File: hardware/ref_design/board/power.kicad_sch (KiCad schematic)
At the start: 25 parts, among them Q1 2N7002, U3 ME6211C33M5G

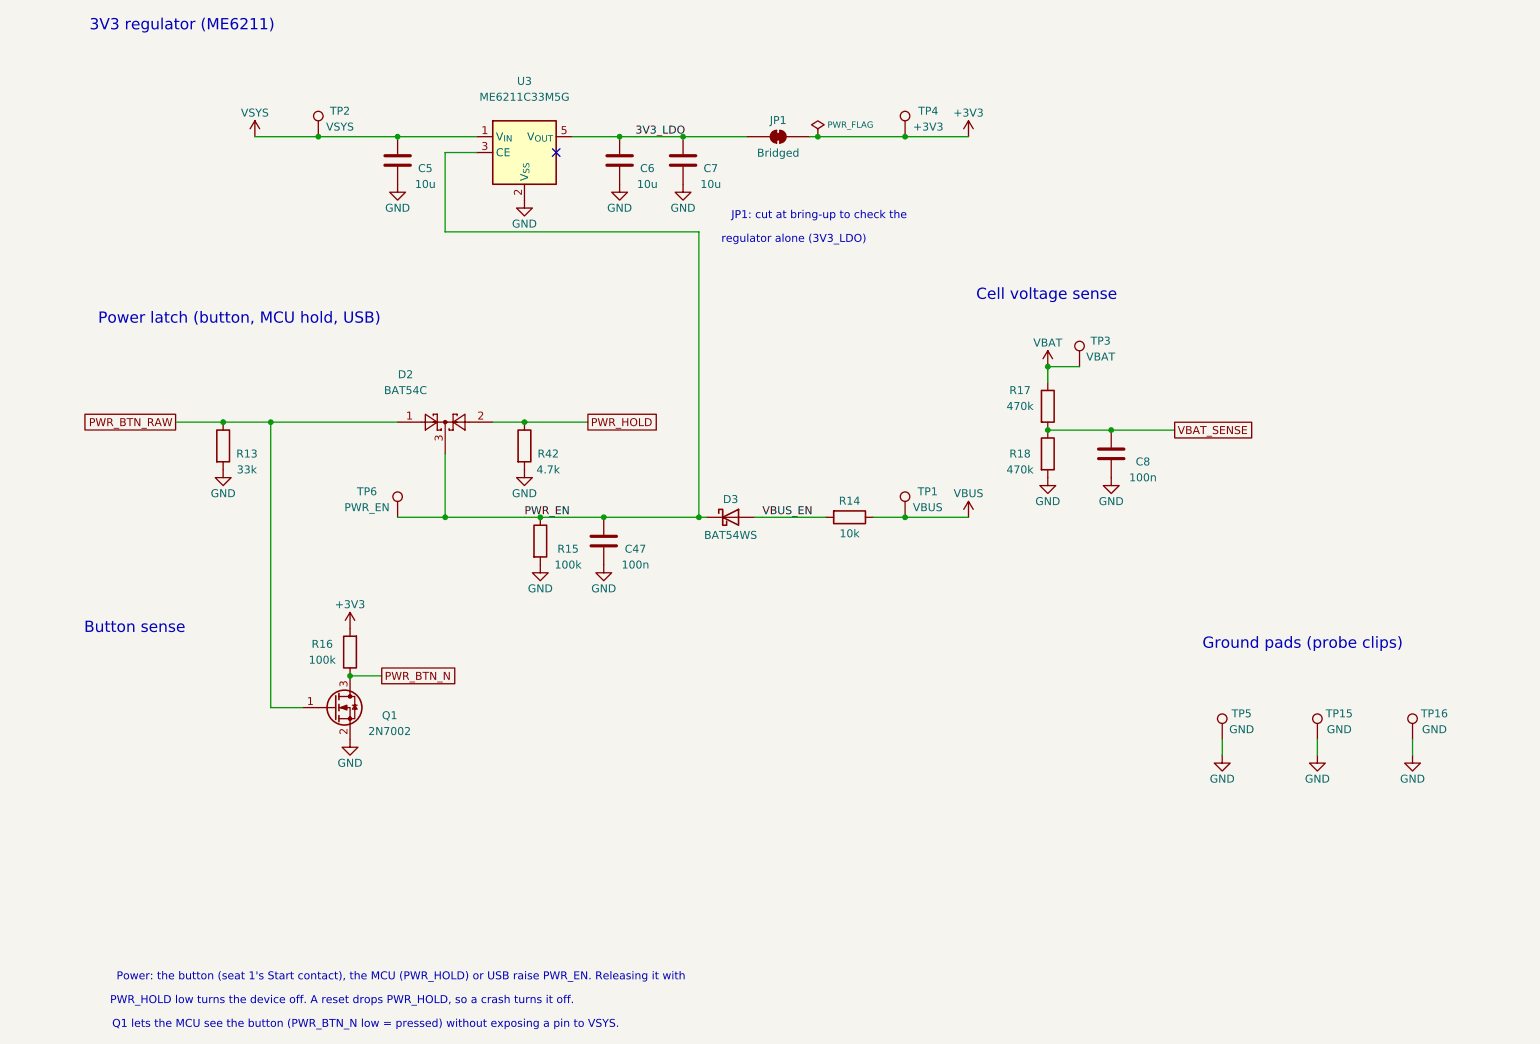
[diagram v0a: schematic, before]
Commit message: WIP: row 19 with shift registers and rows 1, 4, 16; 2 nets unrouted
The cell in a 54.0 x 37.0 mm hole, no speaker, every machine-placed part on
the top. New since the last WIP: each seat's D-pad and A/B/X/Y through a
74HC165 (SN74HC165PWR, chained, SR_PL/SR_CLK/SR_DATA on GPIO28-30, 10k
arrays); seat 2's Start powers on too (D8, R62, Q7, R63; P2_START on
GPIO34); Start/Select on 4 mm metal dome footprints; the BQ24073 power-path
charger in place of the TP4056 and its load sharing (pin reviews written);
the LDO beside the core; side screws at case (+-31.4, +-36); J1 at case
y -11. GPIO8 and GPIO11 (audio) unconnected.

Checks: check_netlist, check_pins and ERC pass (0). DRC: 0 errors, 8
cosmetic silkscreen warnings, 2 unconnected: QSPI_SS (U4 pin 75 to its
3.5 mm stub) and P1_SELECT (U4 pin 44 to SW20). check_fit: 17, all from
the case not knowing the moved screws, J1 and the dome vents yet.

Co-Authored-By: Claude Opus 5.5 <noreply@anthropic.com>
Claude-Session: https://claude.ai/code/session_01Y3mFMxLYqNeyyedvbYuRwX
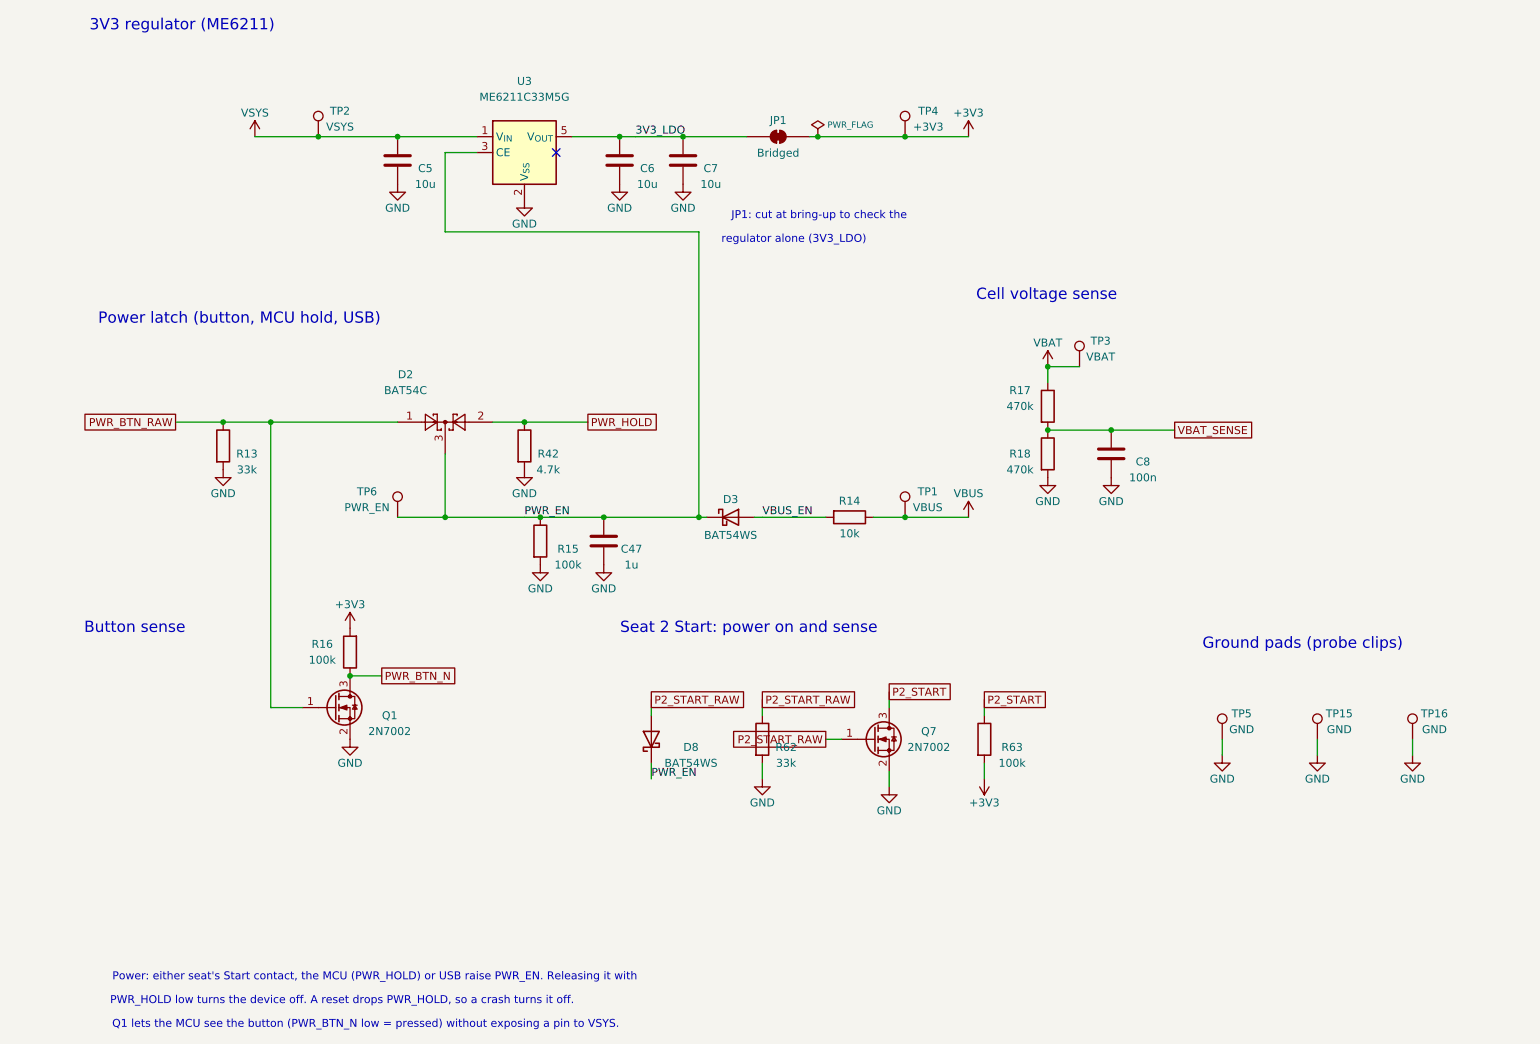
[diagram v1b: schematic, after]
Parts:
- added D8: BAT54WS, Diode_SMD:D_SOD-323, symbol Device:D_Schottky
- added Q7: 2N7002, Package_TO_SOT_SMD:SOT-23, symbol Transistor_FET:2N7002
- added R62: 33k, Resistor_SMD:R_0402_1005Metric, symbol Device:R
- added R63: 100k, Resistor_SMD:R_0402_1005Metric, symbol Device:R
- C47: value 100n -> 1u; LCSC C1525 -> C52923; MPN CL05B104KO5NNNC -> CL05A105KA5NQNC
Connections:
- net +3V3: now also R63.2
- net GND: now also Q7.2 (S), R62.2
- net PWR_EN: now also D8.1 (K)
- new net P2_START: Q7.3 (D), R63.1
- new net P2_START_RAW: D8.2 (A), Q7.1 (G), R62.1
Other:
- note added: "Power: either seat's Start contact, the MCU (PWR_HOLD) or USB raise PWR_EN. Releasing it with"
- note added: "Seat 2 Start: power on and sense"
- note removed: "Power: the button (seat 1's Start contact), the MCU (PWR_HOLD) or USB raise PWR_EN. Releasing it with"

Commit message: ref_design: U1 back to Semtech's SRV05-4.TCT, U3 the RT9013-33GB (JLC stock, no pre-orders)
For a 30-board JLC order with no pre-ordered parts (Alex, 2026-10-22):
- U1 USB ESD: SRV05-4A C20615829 -> Semtech SRV05-4.TCT C13612 (Extended, about 102k in
  stock). Same pinout per Semtech's datasheet (I/O 1, 3, 4, 6; GND 2; REF 5). JLC's
  footprint for C13612 is KiCad's SOT-23-6 turned 180 degrees: assembly.md says so.
- U3 3V3 LDO: ME6211C33M5G-N C82942 -> Richtek RT9013-33GB C47773 (Extended, about 311k).
  Same SOT-23-5 pinout (DS9013-10: pin 4 NC, no BP on this revision). VIN 5.5 V vs VSYS
  <= 4.5 V (BQ24073 OUT 4.3-4.5 V); EN 1.6 V high, 6 V absolute; 1 uF minimum caps.
  Same JLC footprint as C82942.
- J5/J6 not swapped: the Megastar ZX-SH1.0-3PWT clone's land pattern and body differ from
  the SM03B-SRSS-TB footprint (reported, not changed).

design.py, pin reviews, sheet headings, docs; sync_pcb now copies the value too. The board
took the new fields through sync_pcb only: copper unchanged, DRC 0 errors, 0 unconnected,
0 parity issues.

Co-Authored-By: Claude Opus 5.5 <noreply@anthropic.com>
Claude-Session: https://claude.ai/code/session_01Y3mFMxLYqNeyyedvbYuRwX
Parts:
- U3: value ME6211C33M5G -> RT9013-33GB; LCSC C82942 -> C47773; MPN ME6211C33M5G-N -> RT9013-33GB; Manufacturer MICRONE -> Richtek
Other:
- note added: "3V3 regulator (RT9013)"
- note removed: "3V3 regulator (ME6211)"
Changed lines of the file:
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@@
 		)
 	)
-	(text "3V3 regulator (ME6211)"
-		(exclude_from_sim no)
-		(at 34.0655 25.4 0)
+	(text "3V3 regulator (RT9013)"
+		(exclude_from_sim no)
+		(at 33.8081 25.4 0)
 		(effects
 			(font
@@
 			)
 		)
-		(property "Value" "ME6211C33M5G"
+		(property "Value" "RT9013-33GB"
 			(at 88.9 36.83 0)
 			(show_name no)
@@
 			)
 		)
-		(property "LCSC" "C82942"
-			(at 88.9 45.72 0)
-			(hide yes)
-			(show_name no)
-			(do_not_autoplace no)
-			(effects
-				(font
-					(size 1.27 1.27)
-				)
-			)
-		)
-		(property "MPN" "ME6211C33M5G-N"
-			(at 88.9 45.72 0)
-			(hide yes)
-			(show_name no)
-			(do_not_autoplace no)
-			(effects
-				(font
-					(size 1.27 1.27)
-				)
-			)
-		)
-		(property "Manufacturer" "MICRONE"
-			(at 88.9 45.72 0)
-			(hide yes)
+		(property "LCSC" "C47773"
+			(at 88.9 45.72 0)
+			(hide yes)
+			(show_name no)
+			(do_not_autoplace no)
+			(effects
+				(font
+					(size 1.27 1.27)
+				)
+			)
+		)
+		(property "MPN" "RT9013-33GB"
+			(at 88.9 45.72 0)
+			(hide yes)
+			(show_name no)
+			(do_not_autoplace no)
+			(effects
+				(font
+					(size 1.27 1.27)
+				)
+			)
+		)
+		(property "Manufacturer" "Richtek"
+			(at 88.9 45.72 0)
+			(hide yes)

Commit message: ref_design V&V round 3, schematic: R61 3.74k (DEC-31), R14 47k and R43 220k with no clamp (DEC-17), RN1-RN4 47k (DEC-24), U10 buffer on VBAT_SENSE, 10k B4460 NTC for TH1, J4 JST SH, pin reviews
Co-Authored-By: Claude Sonnet 5.5 <noreply@anthropic.com>
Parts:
- added C54: 100n, Capacitor_SMD:C_0402_1005Metric, symbol Device:C
- added U10: MCP6001, Package_TO_SOT_SMD:SOT-23-5, symbol Amplifier_Operational:MCP6L91T-EOT
- R14: value 10k -> 47k; LCSC C25744 -> C25792; MPN 0402WGF1002TCE -> 0402WGF4702TCE
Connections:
- net +3V3: now also C54.1, U10.5 (V+)
- net GND: now also C54.2, U10.2 (V-)
- net VBAT_SENSE: now also U10.1, U10.4 (-); no longer C8.1, R17.2, R18.1
- new net VBAT_DIV: C8.1, R17.2, R18.1, U10.3 (+)

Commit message: ref_design ESP32-S3 schematic: WROOM-1U-N16R8 module, TLV75733P, 8-bit 8080 panel bus (R70-R78), microSD sheet, third 74HC165, BOOT/RESET and J7 pads, 1.5k audio filter; ERC 0, netlist and pin reviews pass
Footprints: battler:ESP32-S3-WROOM-1U (KiCad's without the 0.2 mm thermal vias, tools/fp_esp32.py) and the 4-pad J7. docs/esp32s3_pinmap_diff.md lists the differences from the proposal (no GPIO differs). Unverified: JLC Basic/Extended and stock of the new parts, the DM3AT card-detect pin order.

Co-Authored-By: Claude Sonnet 5.5 <noreply@anthropic.com>
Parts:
- U3: value RT9013-33GB -> TLV75733PDBVR; LCSC C47773 -> C485517; MPN RT9013-33GB -> TLV75733PDBVR; Manufacturer Richtek -> Texas Instruments
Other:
- note added: "3V3 regulator (TLV75733P)"
- note removed: "3V3 regulator (RT9013)"
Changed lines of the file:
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@@
 	(title_block
 		(title "3V3 regulator, power latch, cell voltage sense")
-		(rev "1")
+		(rev "2")
 		(company "Two-player handheld: reference design (REF-A)")
 		(comment 1 "Generated from board/design.py by tools/build_sch.py: edit design.py, not this sheet")
@@
 		)
 	)
-	(text "3V3 regulator (RT9013)"
-		(exclude_from_sim no)
-		(at 33.8081 25.4 0)
+	(text "3V3 regulator (TLV75733P)"
+		(exclude_from_sim no)
+		(at 36.1652 25.4 0)
 		(effects
 			(font
@@
 			)
 		)
-		(property "Value" "RT9013-33GB"
+		(property "Value" "TLV75733PDBVR"
 			(at 88.9 36.83 0)
 			(show_name no)
@@
 			)
 		)
-		(property "LCSC" "C47773"
+		(property "LCSC" "C485517"
 			(at 88.9 45.72 0)
 			(hide yes)
@@
 			)
 		)
-		(property "MPN" "RT9013-33GB"
+		(property "MPN" "TLV75733PDBVR"
 			(at 88.9 45.72 0)
 			(hide yes)
@@
 			)
 		)
-		(property "Manufacturer" "Richtek"
+		(property "Manufacturer" "Texas Instruments"
 			(at 88.9 45.72 0)
 			(hide yes)

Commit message: ref_design ESP32-S3: dedicated power button SW24 (ROCPU TPS850 J14K), Starts plain buttons to GND (P1 Start on U11 bit 22), Q7/D8/R62 removed, R88 added, R63 47k; router keep-outs for the antenna and the microSD footprint's no-trace areas, check_pcb fails on non-silk warnings, silk marker; ERC 0, netlist and pin reviews pass
Co-Authored-By: Claude Sonnet 5.5 <noreply@anthropic.com>
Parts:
- removed D8: BAT54WS, Diode_SMD:D_SOD-323, symbol Device:D_Schottky
- removed Q7: 2N7002, Package_TO_SOT_SMD:SOT-23, symbol Transistor_FET:2N7002
- removed R62: 33k, Resistor_SMD:R_0402_1005Metric, symbol Device:R
- removed R63: 100k, Resistor_SMD:R_0402_1005Metric, symbol Device:R
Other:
- note added: "Power: the power button (SW24, Buttons sheet), the MCU (PWR_HOLD) or USB raise PWR_EN. Releasing it with"
- note removed: "Power: either seat's Start contact, the MCU (PWR_HOLD) or USB raise PWR_EN. Releasing it with"
- note removed: "Seat 2 Start: power on and sense"
